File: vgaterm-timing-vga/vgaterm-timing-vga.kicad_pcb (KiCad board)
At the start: 2 copper layers, 78.7 x 53.8 mm, 48 parts, among them J1 Conn_01x15, J2 Conn_01x08, J3 DE15_Receptacle_HighDensity_M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, J4 Conn_01x03_Pin, J5 Conn_01x02_Pin, J6 Conn_01x03_Pin, J7 Conn_01x02_Pin, U1 74LS161, U2 74LS161, U3 28C256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

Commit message: updating board based on convos with Seth
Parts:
- added J8: Conn_01x04, Connector_Molex:Molex_PicoBlade_53261-0471_1x04-1MP_P1.25mm_Horizontal, B.Cu at (130.0, 70.1)
- moved H3 17.8 mm to (122.4, 72.9)
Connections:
- J3 pad 13: /HSYNC_{2} -> /HSYNC_{3}
- J3 pad 14: /VSYNC_{2} -> /VSYNC_{3}
- U9 pad 16: /VSYNC_{2} -> /VSYNC_{3}
- U9 pad 17: /HSYNC_{2} -> /HSYNC_{3}
- U9 pad 6: GND -> /HSYNC_{2}
- U9 pad 7: GND -> /VSYNC_{2}
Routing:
- net /R2: track 16.6 -> 55.5 mm, vias 1 -> 2
- net /VSYNC_{3}: track 0.00 -> 25.2 mm, vias 0 -> 1
- net /VSYNC_{2}: track 25.2 -> 0.00 mm, vias 1 -> 0
- net /HSYNC_{3}: track 0.00 -> 22.7 mm
- net /HSYNC_{2}: track 22.7 -> 0.00 mm
- net /B2: track 5.37 -> 26.7 mm
- net /G2: track 3.20 -> 24.5 mm
- net /Vis: track 105.2 -> 100.5 mm
- net GND: track 57.9 -> 61.7 mm, vias 15 -> 16
- net Net-(R13-Pad1): track 4.81 -> 7.35 mm
- net /P7: track 26.2 -> 27.9 mm
- net /KBTx: track 48.3 -> 49.5 mm
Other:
- outline, holes or cut-outs redrawn
- board text added: "RGB"

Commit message: updating timing board hsync vsync delay
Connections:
- U9 pad 14: unconnected-(U9-Q5-Pad14) -> /VSYNC_{3}
- U9 pad 15: unconnected-(U9-Q4-Pad15) -> /HSYNC_{3}
- U9 pad 16: /VSYNC_{3} -> /VSYNC_{2}
- U9 pad 17: /HSYNC_{3} -> /HSYNC_{2}
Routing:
- net /VSYNC_{2}: track 0.00 -> 10.8 mm
- net /HSYNC_{2}: track 0.00 -> 10.8 mm
- net /HSYNC_{3}: track 22.7 -> 26.4 mm
- net /VSYNC_{3}: track 25.2 -> 28.7 mm
- net GND: track 61.7 -> 59.2 mm

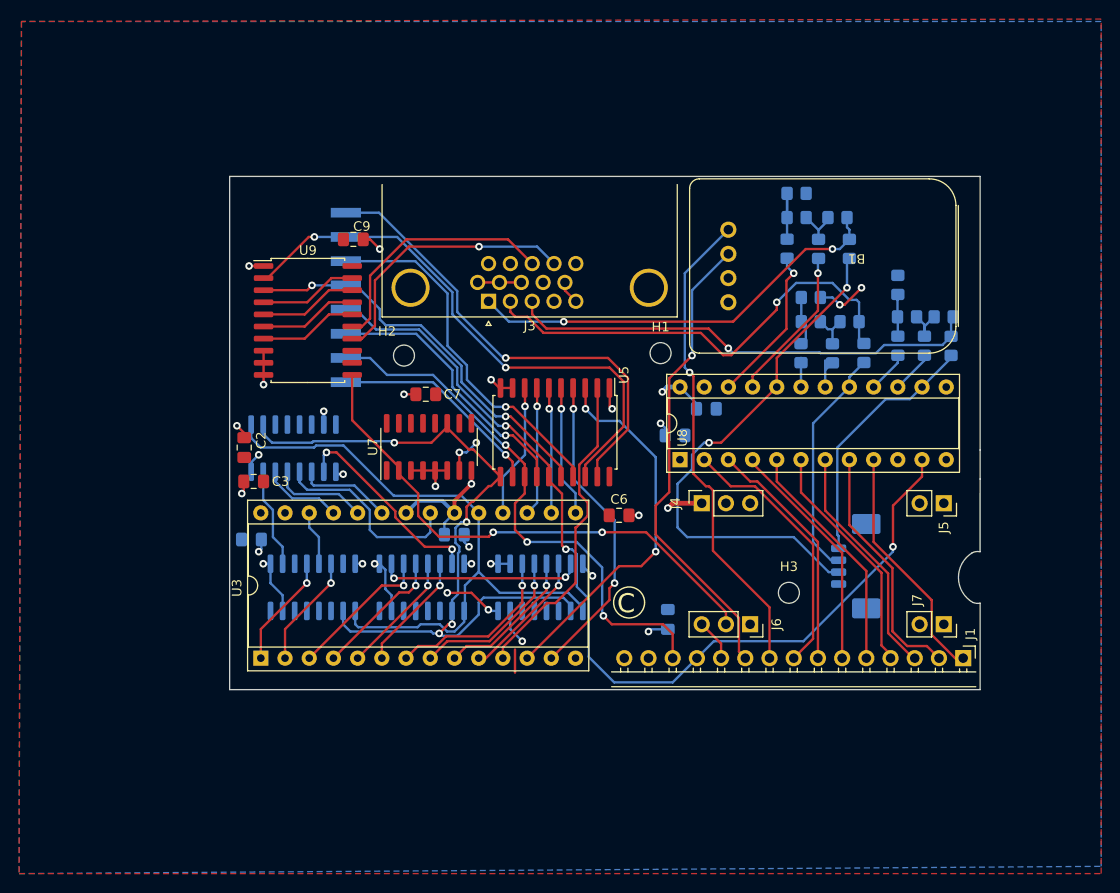
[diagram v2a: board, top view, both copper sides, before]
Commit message: timing board updates and adding keyboard loft board and vga breakout
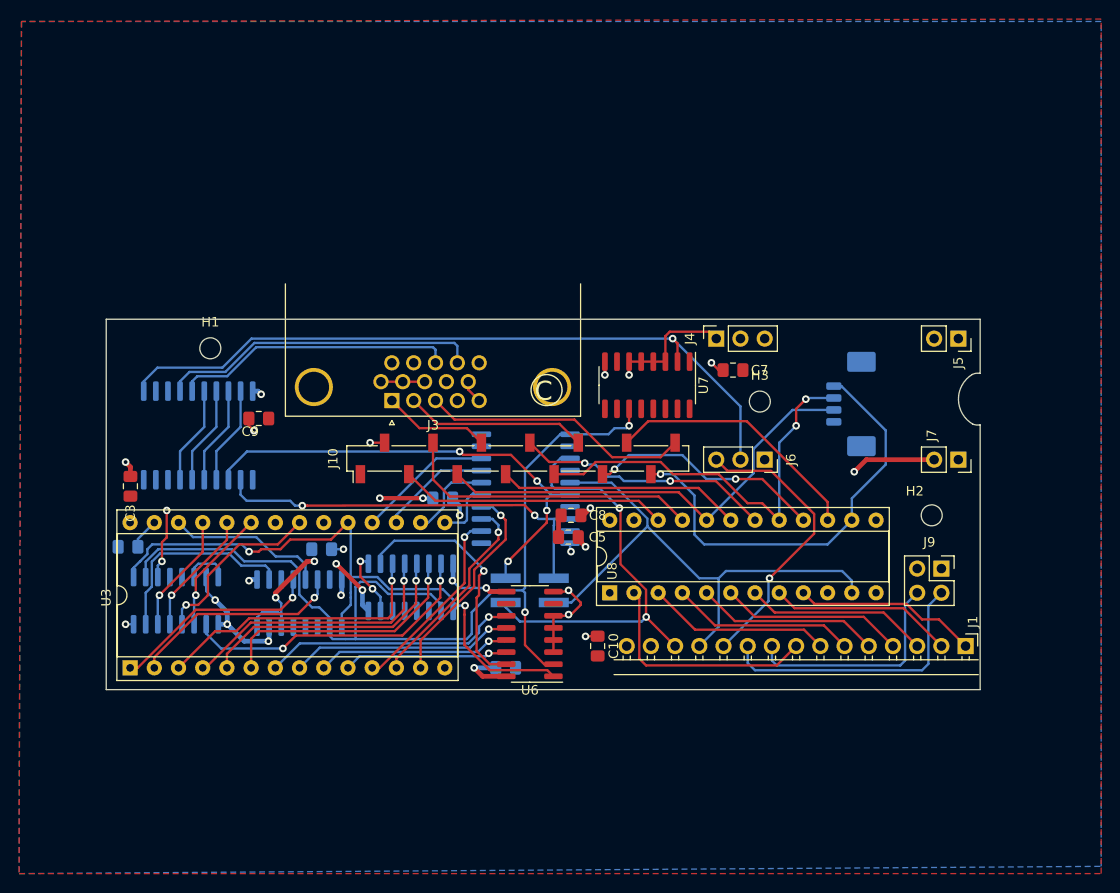
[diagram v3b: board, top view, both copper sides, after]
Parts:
- removed B1: ~, local:USB-UART-board
- removed R1, R10, R12, R13, R14, R16, R18, R2, R4, R6, R7, R8: 2R, Resistor_SMD:R_0805_2012Metric_Pad1.20x1.40mm_HandSolder
- removed R11, R15, R17, R3, R5, R9: R, Resistor_SMD:R_0805_2012Metric_Pad1.20x1.40mm_HandSolder
- added J10: Conn_01x14, Connector_PinSocket_2.54mm:PinSocket_1x14_P2.54mm_Vertical_SMD_Pin1Left, F.Cu at (94.0, 58.8)
- added J9: Conn_01x04, Connector_PinSocket_2.54mm:PinSocket_2x02_P2.54mm_Vertical, F.Cu at (138.4, 70.4)
- C10, C5, C8, U6: moved to F.Cu
- C2, C6, U5, U9: moved to B.Cu
- J2: value Conn_01x08 -> Conn_01x04; footprint local:M208890845 -> Connector_PinHeader_2.54mm:PinHeader_2x02_P2.54mm_Vertical_SMD
- moved H2 57.9 mm to (137.4, 64.8)
- moved H1 47.2 mm to (61.7, 47.2)
- moved J2 38.3 mm to (95.2, 72.6), turned to 180 degrees
- moved C7 32.3 mm to (116.6, 49.5)
- moved U7 23.8 mm to (107.6, 51.1), turned to -90 degrees
- moved C9 21.3 mm to (66.8, 54.6), turned to 180 degrees
- moved H3 20.3 mm to (119.4, 52.8)
- moved U2 20.2 mm to (58.1, 73.7)
- moved C6 19.9 mm to (92.7, 80.8)
- moved C8 18.1 mm to (99.6, 64.8)
- moved J4 17.3 mm to (114.8, 46.2)
- moved J6 17.3 mm to (119.9, 58.9)
- moved J7 17.3 mm to (140.2, 58.9)
- moved J5 17.3 mm to (140.2, 46.2)
- moved J8 17.0 mm to (129.5, 53.1)
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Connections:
- J2 pad 1: /HVis -> /HSync
- J2 pad 2: /HSync -> /Vsync
- J2 pad 3: /VertVis -> /Vis
- J2 pad 4: /Vsync -> /~{StartFrame}
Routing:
- net /HVis: track 49.8 -> 0.00 mm, vias 1 -> 0
- net /Vis: track 100.5 -> 57.3 mm, vias 3 -> 0
- net /VertVis: track 37.9 -> 0.00 mm, vias 1 -> 0
- net /ARed: track 44.7 -> 11.2 mm, vias 2 -> 0
- net GND: track 59.2 -> 91.4 mm, vias 16 -> 20
- net /AGreen: track 48.5 -> 19.1 mm, vias 1 -> 0
- net /~{Vis}: track 28.3 -> 0.00 mm, vias 1 -> 0
- net /KBRx: track 50.7 -> 23.6 mm, vias 1 -> 0
- net /~{A_{out}}: track 4.40 -> 30.4 mm, vias 0 -> 1
- net /CLK_{sync}: track 79.0 -> 104.3 mm, vias 4 -> 2
- net /G1: track 3.87 -> 27.0 mm, vias 0 -> 2
- net /B1: track 4.49 -> 27.4 mm
- net /Othr: track 22.5 -> 0.00 mm, vias 1 -> 0
- net /G0: track 3.78 -> 25.6 mm
- net /ABlue: track 49.9 -> 28.2 mm, vias 1 -> 0
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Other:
- board size 78.7 x 53.8 mm -> 91.7 x 38.9 mm

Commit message: timing board routed and labeled with no errors
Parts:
- moved H1 16.4 mm to (71.1, 60.7)
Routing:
- net /CLK_{sync}: track 104.3 -> 92.0 mm
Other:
- board text added: "B"
- board text added: "Blue"
- board text added: "Clk"
- board text added: "D.HSync"
- board text added: "D.VSync"
- board text added: "DAC"
- board text added: "Green"
- board text added: "KB"
- board text added: "Red"
- board text added: "VSync"
- board text added: "~{Clk}"
- board text removed: "HVis"
- board text removed: "Othr"
- board text removed: "VertVis"
- board text removed: "Vsync"
- board text removed: "~{Vis}"

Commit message: current boards
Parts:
- J3: footprint Connector_Dsub:DSUB-15-HD_Female_Horizontal_P2.29x1.98mm_EdgePinOffset8.35mm_Housed_MountingHolesOffset10.89mm -> local:DSUB-15-HD_Female_Horizontal_P2.29x2.54mm_EdgePinOffset8.35mm_Housed_MountingHolesOffset10.89mm
- moved J3 0.38 mm to (80.7, 53.1)
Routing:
- net GND: track 91.0 -> 97.1 mm
